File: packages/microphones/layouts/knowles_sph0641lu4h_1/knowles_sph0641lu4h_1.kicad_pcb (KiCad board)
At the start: 2 copper layers, 3 parts

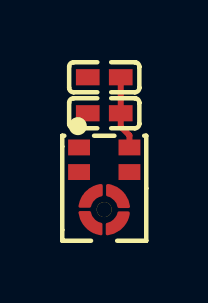
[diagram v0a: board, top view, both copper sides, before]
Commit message: Upgrade Packages: Narayans Half (#185)
* adi-ad5693r

* fix frozen

* prjc-teensy_4_1

* rp2040

* adi-adxl375: Add missing usage build target to ato.yaml

* adi-ds2482s-800: Update layout files after build

* adi-ltc4311: Update layout to fix frozen build

- Updated net names (BUS1/BUS2 → SDA/SCL, gnd → GND, hv → VCC)
- Fixed footprint properties and coordinates
- Package now passes frozen build and verification

* awinic-aw9523: Update layout to fix frozen build

- Updated net names (AD0/AD1 → address_bit_0/address_bit_1, hv → VCC, gnd → GND)
- Updated GPIO line names (-line-0 → gpios[8]-line, etc.)
- Fixed footprint properties and coordinates
- Package now passes frozen build and verification

* awinic-aw9523: Bump version to 0.1.1

- Version bump due to layout updates to fix frozen build

* adi-adbms6830: Fix package verify issues

- Add has_part_removed trait to components missing pickers (atopile_logo, SPDT, analog_DPDT)
- Add missing import for has_part_removed trait
- Add exclude_checks to usage build in ato.yaml
- Update README.md to match usage.ato content
- Bump version from 0.1.2 to 0.1.3

Package now passes ato package verify -s

* indicator-leds: Update layout and bump version

- Updated PCB layout coordinates to fix frozen build issues
- Bumped version from 0.1.5 to 0.1.6
- Package now passes ato package verify -s successfully

* Bump package versions for done packages

- adi-adxl345: 0.1.1 -> 0.1.2
- adi-adxl375: 0.1.0 -> 0.1.1
- adi-ds2482s-800: 0.1.0 -> 0.1.1
- adi-ltc4311: 0.1.0 -> 0.1.1
- adi-ltc4316: 0.1.0 -> 0.1.1
- ams-tsl2591: 0.1.0 -> 0.1.1

These packages were marked as 'Done' in package-todos.md but had version
warnings during package verification. Version bumps ensure they can be
published to the registry.

* invensense-mpu6050: Update layout files and bump version to 0.1.2

* Fix picker warnings by adding has_part_removed trait to MCU modules

- Added #pragma experiment("TRAITS") to enable traits feature
- Added import has_part_removed t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
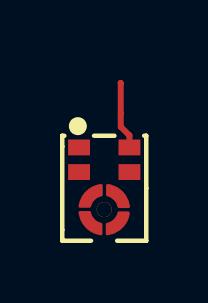
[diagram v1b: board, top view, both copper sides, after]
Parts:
- removed C1: 100nF ±10% 16V X7R, Samsung_Electro_Mechanics_CL05B104KO5NNNC:C0402
- removed C2: 220pF ±10% 50V X7R, FH_0402B221K500NT:C0402
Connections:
- net CLOCK renamed SCK
- net DATA renamed SD
- net SELECT renamed WS
- U1 pad 3: gnd -> GND
- U1 pad 5: VDD -> VCC
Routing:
- net VDD: track 2.46 -> 0.00 mm
- net VCC: track 0.00 -> 2.27 mm

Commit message: review tool updates
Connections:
- net GND renamed lv
- net VCC renamed hv
- U1 pad : net -> (no net)

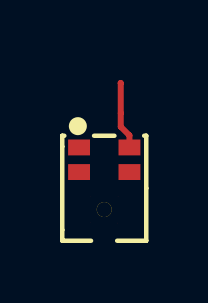
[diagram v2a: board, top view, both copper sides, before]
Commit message: remove all those other changes, just bosch baby
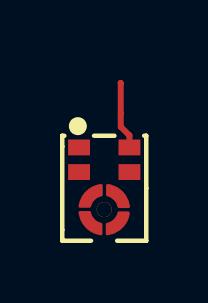
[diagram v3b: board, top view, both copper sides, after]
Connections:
- net hv renamed VCC
- net lv renamed GND
- U1 pad : (no net) -> net
